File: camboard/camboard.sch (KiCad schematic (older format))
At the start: 30 parts

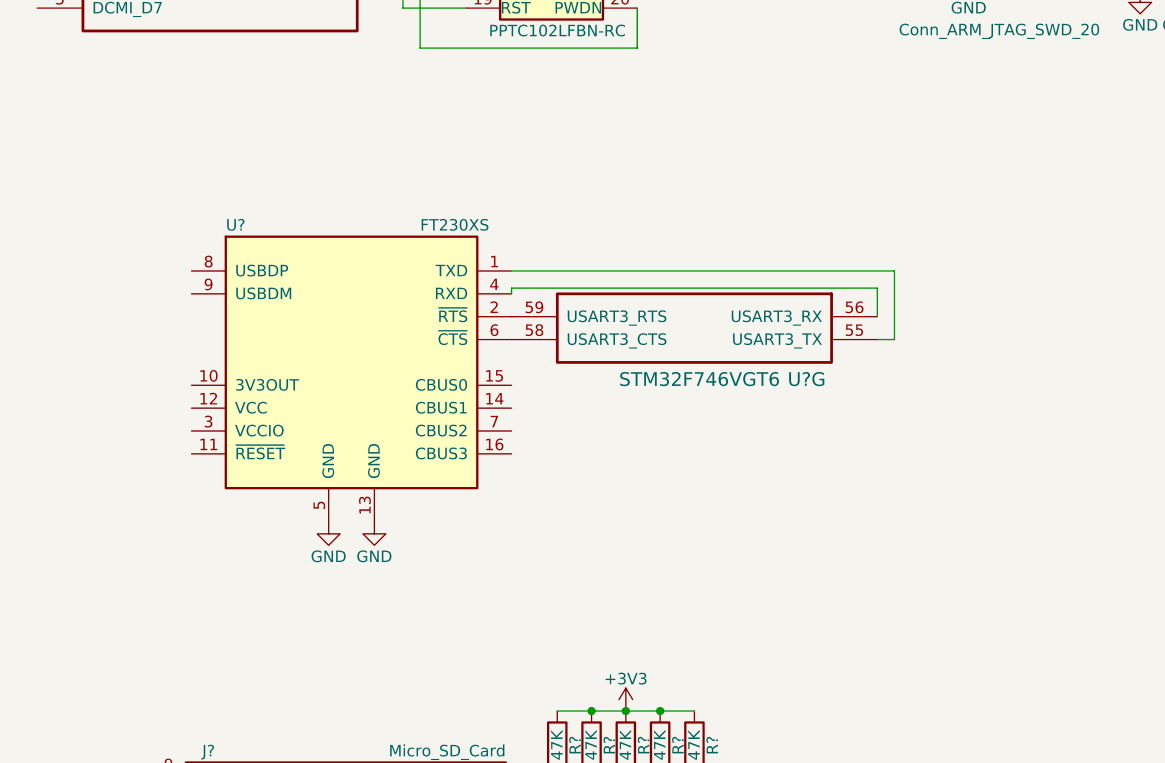
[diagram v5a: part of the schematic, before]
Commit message: added usb-uart
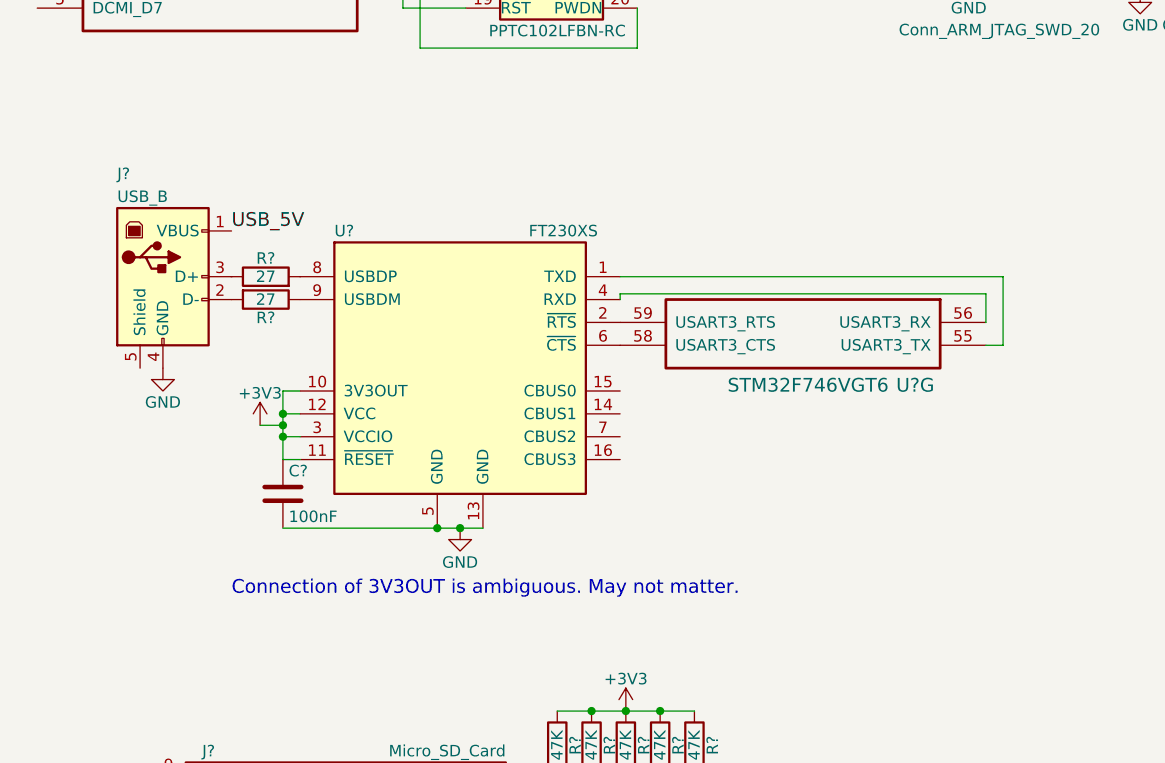
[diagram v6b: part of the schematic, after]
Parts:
- added C?: 100nF, symbol C
- added J?: USB_B, symbol USB_B
- added R? (x2): 27, symbol R
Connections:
- net +3V3: now also U?.10 (3V3OUT), U?.11 (~RESET), U?.12 (VCC), U?.3 (VCCIO), C?.1
- net GND: now also C?.2, J?.4 (GND)
- net USB_5V: now also J?.1 (VBUS)
- net at U?.8 (USBDP): now also R?.2
- net at U?.9 (USBDM): now also R?.1
- new net: J?.2 (D-), R?.2
- new net: J?.3 (D+), R?.1
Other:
- note added: "Connection of 3V3OUT is ambiguous. May not matter."
- moved on the sheet: U?, U?G
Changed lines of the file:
@@
 L STM32F746VGT6 U?
 U 7 1 59CAFE6F
-P 4200 4075
-F 0 "U?" H 4425 3800 60  0000 L CNN
-F 1 "STM32F746VGT6" H 4625 3800 60  0000 L CNN
-F 2 "" H 4200 4075 60  0001 C CNN
-F 3 "" H 4200 4075 60  0001 C CNN
-	7    4200 4075
+P 4675 4100
+F 0 "U?" H 4900 3825 60  0000 L CNN
+F 1 "STM32F746VGT6" H 5100 3825 60  0000 L CNN
+F 2 "" H 4675 4100 60  0001 C CNN
+F 3 "" H 4675 4100 60  0001 C CNN
+	7    4675 4100
 	-1   0    0    -1
 $EndComp
@@
 L FT230XS U?
 U 1 1 59CBD098
-P 1900 4275
-F 0 "U?" H 1350 4875 50  0000 L CNN
-F 1 "FT230XS" H 2200 4875 50  0000 L CNN
-F 2 "SSOP-16" H 1900 4275 50  0001 C CNN
-F 3 "" H 1900 4275 50  0001 C CNN
-	1    1900 4275
+P 2375 4300
+F 0 "U?" H 1825 4900 50  0000 L CNN
+F 1 "FT230XS" H 2675 4900 50  0000 L CNN
+F 2 "SSOP-16" H 2375 4300 50  0001 C CNN
+F 3 "" H 2375 4300 50  0001 C CNN
+	1    2375 4300
 	1    0    0    -1
 $EndComp
@@
 $Comp
 L GND #PWR?
-U 1 1 59CBCD24
-P 1800 4975
-F 0 "#PWR?" H 1800 4725 50  0001 C CNN
-F 1 "GND" H 1800 4825 50  0000 C CNN
-F 2 "" H 1800 4975 50  0001 C CNN
-F 3 "" H 1800 4975 50  0001 C CNN
-	1    1800 4975
-	1    0    0    -1
-$EndComp
-$Comp
-L GND #PWR?
 U 1 1 59CBCD6B
-P 2000 4975
-F 0 "#PWR?" H 2000 4725 50  0001 C CNN
-F 1 "GND" H 2000 4825 50  0000 C CNN
-F 2 "" H 2000 4975 50  0001 C CNN
-F 3 "" H 2000 4975 50  0001 C CNN
-	1    2000 4975
+P 2375 5000
+F 0 "#PWR?" H 2375 4750 50  0001 C CNN
+F 1 "GND" H 2375 4850 50  0000 C CNN
+F 2 "" H 2375 5000 50  0001 C CNN
+F 3 "" H 2375 5000 50  0001 C CNN
+	1    2375 5000
 	1    0    0    -1
 $EndComp
@@
 	1    0    0    -1
 $EndComp
-Wire Wire Line
-	7700 5375 7375 5375
-Wire Wire Line
-	7375 5375 7375 5825
-Wire Wire Line
-	7675 5825 7700 5825
-Wire Wire Line
-	7700 5825 7700 5675
-Wire Wire Line
-	10000 5525 10450 5525
-Wire Wire Line
-	10000 5825 10450 5825
-Connection ~ 10225 5525
-Connection ~ 10225 5825
-Wire Wire Line
-	9700 5625 9700 5825
-Wire Wire Line
-	2600 3875 4275 3875
-Wire Wire Line
-	4275 3875 4275 4175
-Wire Wire Line
-	4275 4175 4200 4175
-Wire Wire Line
-	4200 4075 4200 3950
-Wire Wire Line
-	4200 3950 2600 3950
-Wire Wire Line
-	2600 3950 2600 3975
-Wire Wire Line
-	2725 6475 3525 6475
-Wire Wire Line
-	2800 6475 2800 6100
-Wire Wire Line
-	2725 6575 3525 6575
-Wire Wire Line
-	2950 6575 2950 6100
-Wire Wire Line
-	2725 6675 3525 6675
-Wire Wire Line
-	3100 6675 3100 6100
-Wire Wire Line
-	2725 6775 3525 6775
-Wire Wire Line
-	3250 6775 3250 6100
-Wire Wire Line
-	2725 6875 3525 6875
-Wire Wire Line
-	3400 6875 3400 6100
-Wire Wire Line
-	2725 6375 3525 6375
-Connection ~ 2800 6475
-Connection ~ 2950 6575
-Connection ~ 3100 6675
-Connection ~ 3250 6775
-Connection ~ 3400 6875
-Wire Wire Line
-	2800 5800 3400 5800
-Connection ~ 2950 5800
-Connection ~ 3100 5800
-Connection ~ 3250 5800
-Wire Wire Line
-	2125 2425 2250 2425
-Wire Wire Line
-	2250 2425 2250 2125
-Wire Wire Line
-	2250 2125 2400 2125
-Wire Wire Line
-	8200 5525 8200 5325
-Wire Wire Line
-	2400 2725 2125 2725
-Wire Wire Line
-	2125 2725 2125 2525
-Wire Wire Line
-	2125 2325 2200 2325
-Wire Wire Line
-	2200 2325 2200 2900
-Wire Wire Line
-	2200 2900 3150 2900
-Wire Wire Line
-	3150 2900 3150 2725
-Wire Wire Line
-	3150 1825 3300 1825
-Wire Wire Line
-	3400 2125 3150 2125
 $Comp
 L +3V3 #PWR?
@@
 	1    0    0    -1
 $EndComp
-Wire Wire Line
-	4600 975  4700 975
-Connection ~ 4650 975
 Text Label 3475 1250 0    60   ~ 0
 NRST
@@
 	1    0    0    -1
 $EndComp
-Wire Wire Line
-	5300 1275 5775 1275
-Wire Wire Line
-	5775 1275 5775 1575
-Wire Wire Line
-	5300 1675 5775 1675
-Wire Wire Line
-	5300 1775 5775 1775
-Wire Wire Line
-	5300 1875 5775 1875
-Wire Wire Line
-	5300 1975 5775 1975
-Wire Wire Line
-	5300 2275 5350 2275
-Wire Wire Line
-	5350 2275 5350 2350
-Wire Wire Line
-	5300 2175 5525 2175
-Wire Wire Line
-	5525 2175 5525 2350
-Wire Wire Line
-	5300 1575 5700 1575
-Wire Wire Line
-	5700 1575 5700 2350
 $Comp
 L GND #PWR?
@@
 Text Notes 4950 1000 0    60   ~ 0
 SRST is connected to "nRSTIN" in user manual.
+$Comp
+L +3V3 #PWR?
+U 1 1 59CD84B9
+P 1500 4550
+F 0 "#PWR?" H 1500 4400 50  0001 C CNN
+F 1 "+3V3" H 1500 4690 50  0000 C CNN
+F 2 "" H 1500 4550 50  0001 C CNN
+F 3 "" H 1500 4550 50  0001 C CNN
+	1    1500 4550
+	1    0    0    -1
+$EndComp
+Text Notes 1375 5300 0    60   ~ 0
+Connection of 3V3OUT is ambiguous. May not matter.
+$Comp
+L USB_B J?
+U 1 1 59CD8F84
+P 1075 3900
+F 0 "J?" H 875 4350 50  0000 L CNN
+F 1 "USB_B" H 875 4250 50  0000 L CNN
+F 2 "" H 1225 3850 50  0001 C CNN
+F 3 "" H 1225 3850 50  0001 C CNN
+	1    1075 3900
+	1    0    0    -1
+$EndComp
+$Comp
+L R R?
+U 1 1 59CD9104
+P 1525 4000
+F 0 "R?" V 1605 4000 50  0000 C CNN
+F 1 "27" V 1525 4000 50  0000 C CNN
+F 2 "" V 1455 4000 50  0001 C CNN
+F 3 "" H 1525 4000 50  0001 C CNN
+	1    1525 4000
+	0    1    1    0
+$EndComp
+$Comp
+L R R?
+U 1 1 59CD91A7
+P 1525 3900
+F 0 "R?" V 1605 3900 50  0000 C CNN
+F 1 "27" V 1525 3900 50  0000 C CNN
+F 2 "" V 1455 3900 50  0001 C CNN
+F 3 "" H 1525 3900 50  0001 C CNN
+	1    1525 3900
+	0    -1   -1   0
+$EndComp
+Text Label 1375 3700 0    60   ~ 0
+USB_5V
+Wire Wire Line
+	7700 5375 7375 5375
+Wire Wire Line
+	7375 5375 7375 5825
+Wire Wire Line
+	7675 5825 7700 5825
+Wire Wire Line
+	7700 5825 7700 5675
+Wire Wire Line
+	10000 5525 10450 5525
+Wire Wire Line
+	10000 5825 10450 5825
+Connection ~ 10225 5525
+Connection ~ 10225 5825
+Wire Wire Line
+	9700 5625 9700 5825
+Wire Wire Line
+	3075 3900 4750 3900
+Wire Wire Line
+	4750 3900 4750 4200
+Wire Wire Line
+	4750 4200 4675 4200
+Wire Wire Line
+	4675 4100 4675 3975
+Wire Wire Line
+	4675 3975 3075 3975
+Wire Wire Line
+	3075 3975 3075 4000
+Wire Wire Line
+	2725 6475 3525 6475
+Wire Wire Line
+	2800 6475 2800 6100
+Wire Wire Line
+	2725 6575 3525 6575
+Wire Wire Line
+	2950 6575 2950 6100
+Wire Wire Line
+	2725 6675 3525 6675
+Wire Wire Line
+	3100 6675 3100 6100
+Wire Wire Line
+	2725 6775 3525 6775
+Wire Wire Line
+	3250 6775 3250 6100
+Wire Wire Line
+	2725 6875 3525 6875
+Wire Wire Line
+	3400 6875 3400 6100
+Wire Wire Line
+	2725 6375 3525 6375
+Connection ~ 2800 6475
+Connection ~ 2950 6575
+Connection ~ 3100 6675
+Connection ~ 3250 6775
+Connection ~ 3400 6875
+Wire Wire Line
+	2800 5800 3400 5800
+Connection ~ 2950 5800
+Connection ~ 3100 5800
+Connection ~ 3250 5800
+Wire Wire Line
+	2125 2425 2250 2425
+Wire Wire Line
+	2250 2425 2250 2125
+Wire Wire Line
+	2250 2125 2400 2125
+Wire Wire Line
+	8200 5525 8200 5325
+Wire Wire Line
+	2400 2725 2125 2725
+Wire Wire Line
+	2125 2725 2125 2525
+Wire Wire Line
+	2125 2325 2200 2325
+Wire Wire Line
+	2200 2325 2200 2900
+Wire Wire Line
+	2200 2900 3150 2900
+Wire Wire Line
+	3150 2900 3150 2725
+Wire Wire Line
+	3150 1825 3300 1825
+Wire Wire Line
+	3400 2125 3150 2125
+Wire Wire Line
+	4600 975  4700 975
+Connection ~ 4650 975
+Wire Wire Line
+	5300 1275 5775 1275
+Wire Wire Line
+	5775 1275 5775 1575
+Wire Wire Line
+	5300 1675 5775 1675
+Wire Wire Line
+	5300 1775 5775 1775
+Wire Wire Line
+	5300 1875 5775 1875
+Wire Wire Line
+	5300 1975 5775 1975
+Wire Wire Line
+	5300 2275 5350 2275
+Wire Wire Line
+	5350 2275 5350 2350
+Wire Wire Line
+	5300 2175 5525 2175
+Wire Wire Line
+	5525 2175 5525 2350
+Wire Wire Line
+	5300 1575 5700 1575
+Wire Wire Line
+	5700 1575 5700 2350
+Wire Wire Line
+	1600 5000 2475 5000
+Connection ~ 2375 5000
+Wire Wire Line
+	1500 4550 1600 4550
+Wire Wire Line
+	1600 4400 1600 4700
+Wire Wire Line
+	1600 4400 1675 4400
+Wire Wire Line
+	1675 4500 1600 4500
+Connection ~ 1600 4500
+Wire Wire Line
+	1600 4600 1675 4600
+Connection ~ 1600 4550
+Wire Wire Line
+	1600 4700 1675 4700
+Connection ~ 1600 4600
+$Comp
+L GND #PWR?
+U 1 1 59CDA5A5
+P 1075 4300
+F 0 "#PWR?" H 1075 4050 50  0001 C CNN
+F 1 "GND" H 1075 4150 50  0000 C CNN
+F 2 "" H 1075 4300 50  0001 C CNN
+F 3 "" H 1075 4300 50  0001 C CNN
+	1    1075 4300
+	1    0    0    -1
+$EndComp
+$Comp
+L C C?
+U 1 1 59CDA945
+P 1600 4850
+F 0 "C?" H 1625 4950 50  0000 L CNN
+F 1 "100nF" H 1625 4750 50  0000 L CNN
+F 2 "" H 1638 4700 50  0001 C CNN
+F 3 "" H 1600 4850 50  0001 C CNN
+	1    1600 4850
+	1    0    0    -1
+$EndComp
+Connection ~ 2275 5000
 $EndSCHEMATC

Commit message: some peripherals are done
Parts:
- added D? (x2): LED, symbol LED
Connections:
- net +3V3: now also D?.2 (A), D?.2 (A)
- net at U?.14 (CBUS1): now also D?.1 (K)
- net at U?.7 (CBUS2): now also D?.1 (K)
- net VIN renamed VBAT
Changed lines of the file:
@@
 $EndComp
 Text Label 825  825  2    60   ~ 0
-VIN
+VBAT
 $Comp
 L GND #PWR?
@@
 $EndComp
 Connection ~ 2275 5000
+$Comp
+L LED D?
+U 1 1 59CDB4C2
+P 5075 4225
+F 0 "D?" H 5075 4325 50  0000 C CNN
+F 1 "LED" H 5075 4125 50  0000 C CNN
+F 2 "" H 5075 4225 50  0001 C CNN
+F 3 "" H 5075 4225 50  0001 C CNN
+	1    5075 4225
+	0    -1   -1   0
+$EndComp
+$Comp
+L LED D?
+U 1 1 59CDB58A
+P 5400 4225
+F 0 "D?" H 5400 4325 50  0000 C CNN
+F 1 "LED" H 5400 4125 50  0000 C CNN
+F 2 "" H 5400 4225 50  0001 C CNN
+F 3 "" H 5400 4225 50  0001 C CNN
+	1    5400 4225
+	0    -1   -1   0
+$EndComp
+$Comp
+L +3V3 #PWR?
+U 1 1 59CDB61C
+P 5075 4075
+F 0 "#PWR?" H 5075 3925 50  0001 C CNN
+F 1 "+3V3" H 5075 4215 50  0000 C CNN
+F 2 "" H 5075 4075 50  0001 C CNN
+F 3 "" H 5075 4075 50  0001 C CNN
+	1    5075 4075
+	1    0    0    -1
+$EndComp
+$Comp
+L +3V3 #PWR?
+U 1 1 59CDB693
+P 5400 4075
+F 0 "#PWR?" H 5400 3925 50  0001 C CNN
+F 1 "+3V3" H 5400 4215 50  0000 C CNN
+F 2 "" H 5400 4075 50  0001 C CNN
+F 3 "" H 5400 4075 50  0001 C CNN
+	1    5400 4075
+	1    0    0    -1
+$EndComp
+Wire Wire Line
+	5075 4375 5075 4500
+Wire Wire Line
+	5075 4500 3075 4500
+Wire Wire Line
+	5400 4375 5400 4600
+Wire Wire Line
+	5400 4600 3075 4600
 $EndSCHEMATC

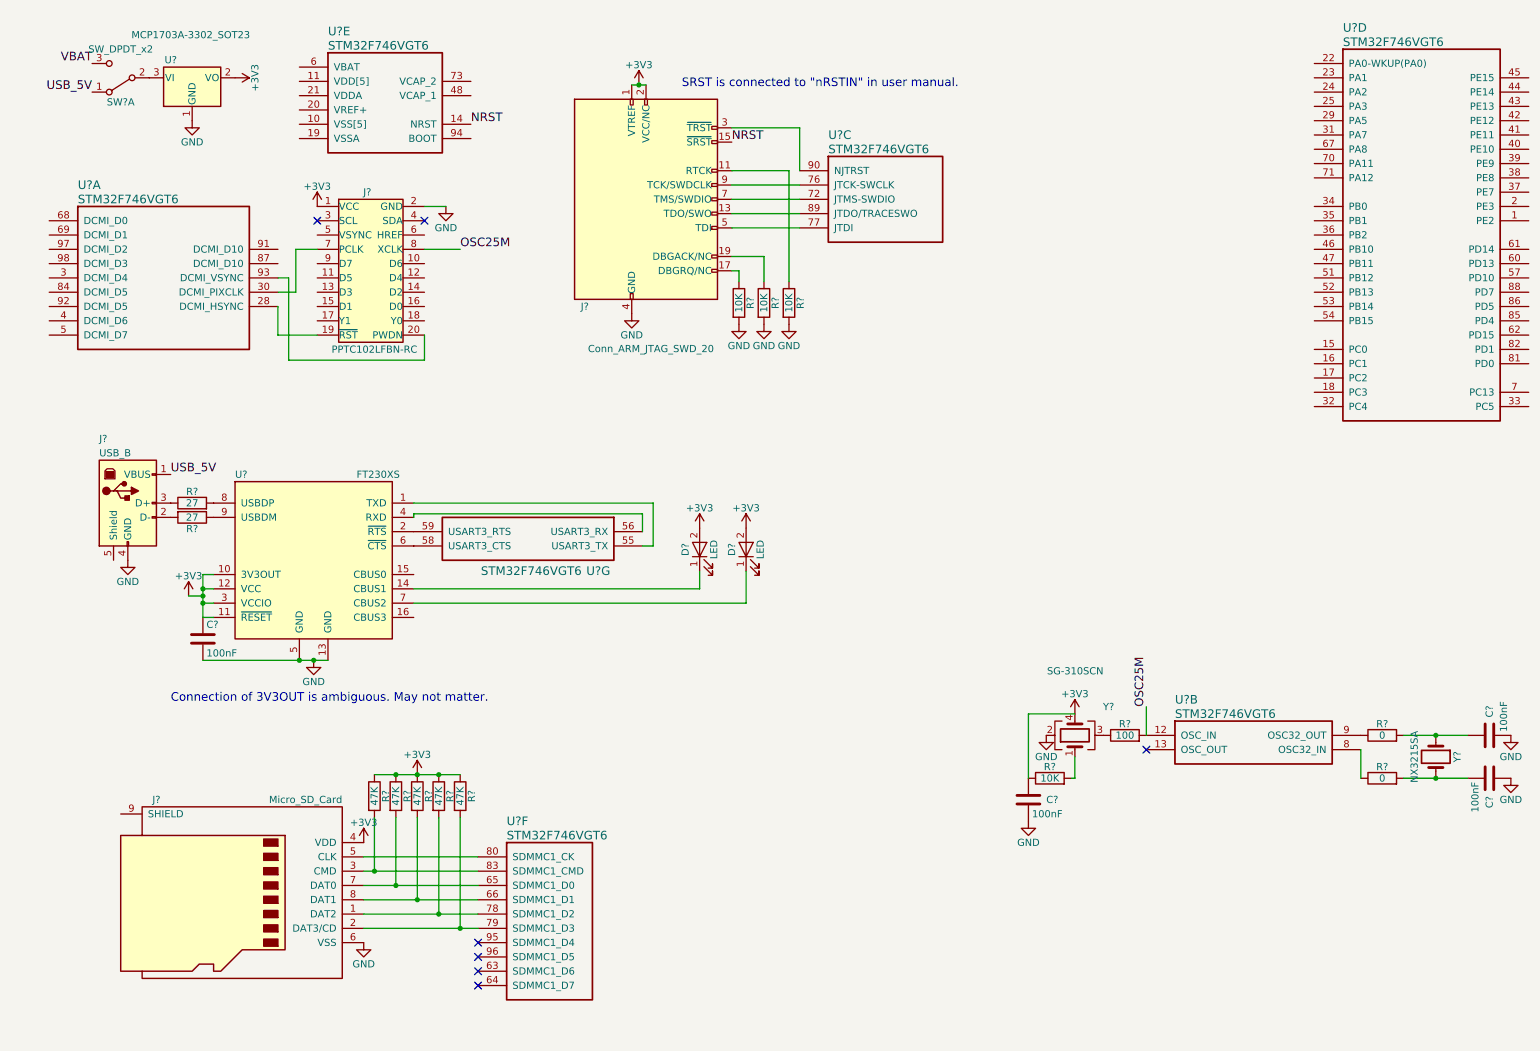
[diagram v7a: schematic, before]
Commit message: added some labels
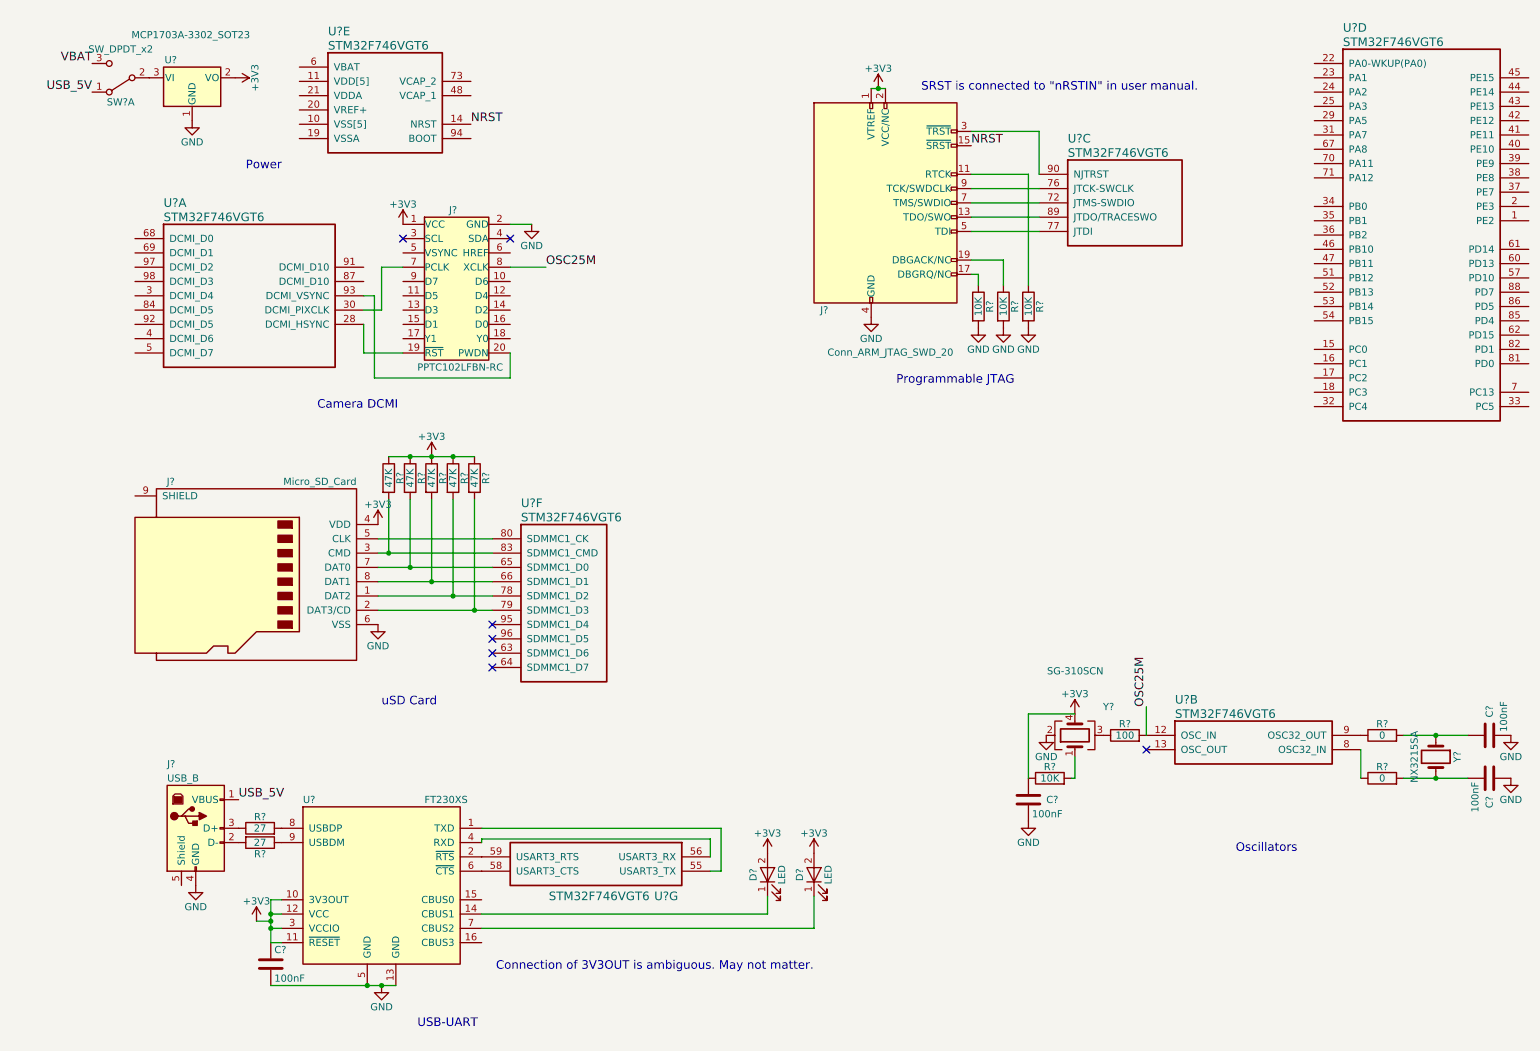
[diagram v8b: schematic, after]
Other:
- note added: "Camera DCMI"
- note added: "Oscillators"
- note added: "Power"
- note added: "Programmable JTAG"
- note added: "USB-UART"
- note added: "uSD Card"
- moved on the sheet: C?, D?, J?, R?, U?, U?A, U?C, U?F, U?G
